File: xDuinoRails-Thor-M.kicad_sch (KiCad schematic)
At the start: 4 parts, among them J1101 Conn_01x10, J1102 Conn_01x10, J1103 Conn_01x10, U1101 MOUDLE-SEEEDUINO-XIAO

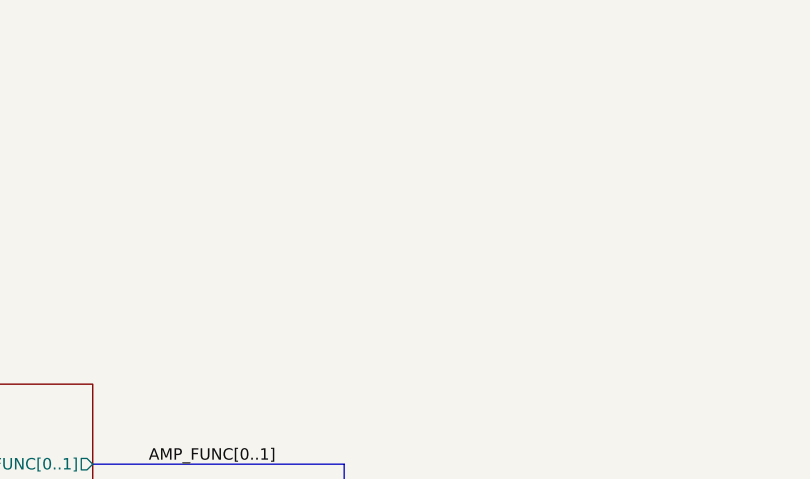
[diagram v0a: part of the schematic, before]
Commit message: Chg - Clearer PCB layout
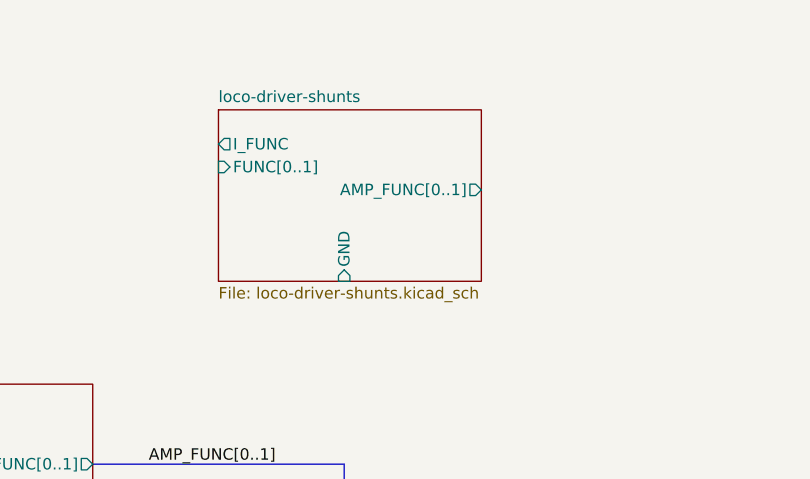
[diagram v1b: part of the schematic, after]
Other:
- added sheet loco-driver-shunts (loco-driver-shunts.kicad_sch)
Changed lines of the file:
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@@
+	)
+	(sheet
+		(at 214.63 41.91)
+		(size 29.21 19.05)
+		(fields_autoplaced yes)
+		(stroke
+			(width 0.1524)
+			(type solid)
+		)
+		(fill
+			(color 255 255 203 1.0000)
+		)
+		(property "Sheetname" "loco-driver-shunts"
+			(at 214.63 41.1984 0)
+			(effects
+				(font
+					(size 1.27 1.27)
+				)
+				(justify left bottom)
+			)
+		)
+		(property "Sheetfile" "loco-driver-shunts.kicad_sch"
+			(at 214.63 61.5446 0)
+			(effects
+				(font
+					(size 1.27 1.27)
+				)
+				(justify left top)
+			)
+		)
+		(pin "GND" input
+			(at 228.6 60.96 270)
+			(effects
+				(font
+					(size 1.27 1.27)
+				)
+				(justify left)
+			)
+		)
+		(pin "I_FUNC" output
+			(at 214.63 45.72 180)
+			(effects
+				(font
+					(size 1.27 1.27)
+				)
+				(justify left)
+			)
+		)
+		(pin "AMP_FUNC[0..1]" output
+			(at 243.84 50.8 0)
+			(effects
+				(font
+					(size 1.27 1.27)
+				)
+				(justify right)
+			)
+		)
+		(pin "FUNC[0..1]" input
+			(at 214.63 48.26 180)
+			(effects
+				(font
+					(size 1.27 1.27)
+				)
+				(justify left)
+			)
+		)
+		(instances
+			(project "xDuinoRails-Thor-M"
+				(path "/fb33ec4e-6596-45d2-a121-8d3475acd69a"
+					(page "1")
+				)
+			)
+		)
 	)
 	(sheet

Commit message: Fix - ERC updates
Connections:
- no-connect marks 6 -> 12
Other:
- sheet loco-driver-shunts ports: added +3V3, I_MOTOR, OFF_ MOTOR, OFF_FUNC; removed AMP_FUNC[0..1], FUNC[0..1]
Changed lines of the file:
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@@
 	)
 	(no_connect
+		(at 229.87 60.96)
+	)
+	(no_connect
+		(at 243.84 52.07)
+	)
+	(no_connect
 		(at 269.24 124.46)
 	)
@@
 	)
 	(no_connect
+		(at 243.84 49.53)
+	)
+	(no_connect
 		(at 269.24 129.54)
 	)
@@
 	)
 	(no_connect
+		(at 214.63 52.07)
+	)
+	(no_connect
 		(at 269.24 121.92)
 	)
 	(no_connect
+		(at 229.87 41.91)
+	)
+	(no_connect
+		(at 214.63 49.53)
+	)
+	(no_connect
 		(at 233.68 133.35)
 	)
@@
 			(project "xDuinoRails-Thor-M"
 				(path "/fb33ec4e-6596-45d2-a121-8d3475acd69a"
-					(page "11")
+					(page "2")
 				)
 			)
@@
 			(project "xDuinoRails-Thor-M"
 				(path "/fb33ec4e-6596-45d2-a121-8d3475acd69a"
-					(page "2")
+					(page "1")
 				)
 			)
@@
 			)
 		)
-		(pin "GND" input
-			(at 228.6 60.96 270)
+		(pin "I_MOTOR" input
+			(at 243.84 52.07 0)
 			(effects
 				(font
 					(size 1.27 1.27)
 				)
-				(justify left)
+				(justify right)
 			)
 		)
-		(pin "I_FUNC" output
-			(at 214.63 45.72 180)
+		(pin "+3V3" input
+			(at 229.87 41.91 90)
+			(effects
+				(font
+					(size 1.27 1.27)
+				)
+				(justify right)
+			)
+		)
+		(pin "GND" input
+			(at 229.87 60.96 270)
 			(effects
 				(font
@@
 			)
 		)
-		(pin "AMP_FUNC[0..1]" output
-			(at 243.84 50.8 0)
+		(pin "I_FUNC" input
+			(at 243.84 49.53 0)
 			(effects
 				(font
@@
 			)
 		)
-		(pin "FUNC[0..1]" input
-			(at 214.63 48.26 180)
+		(pin "OFF_ MOTOR" output
+			(at 214.63 52.07 180)
+			(effects
+				(font
+					(size 1.27 1.27)
+				)
+				(justify left)
+			)
+		)
+		(pin "OFF_FUNC" output
+			(at 214.63 49.53 180)
 			(effects
 				(font
@@
 			(project "xDuinoRails-Thor-M"
 				(path "/fb33ec4e-6596-45d2-a121-8d3475acd69a"
-					(page "1")
+					(page "11")
 				)
 			)

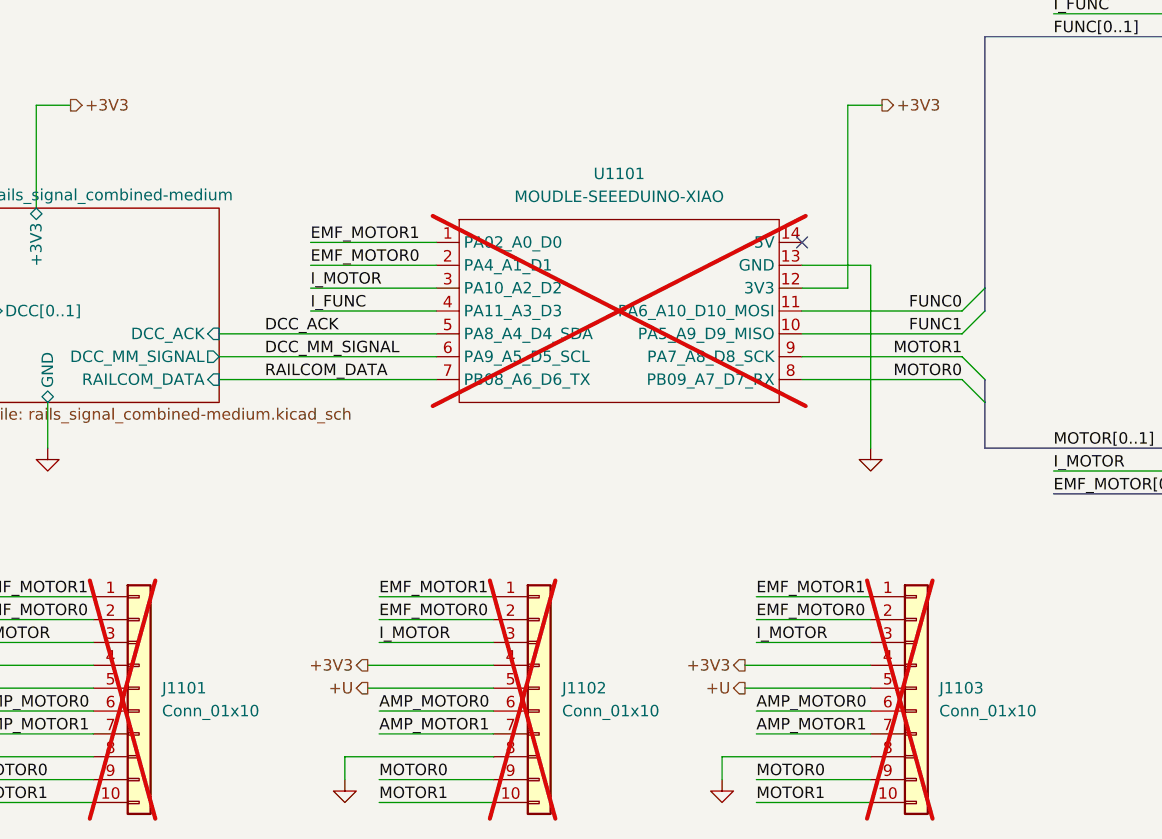
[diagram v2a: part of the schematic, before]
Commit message: Fix - Ignore double power flags
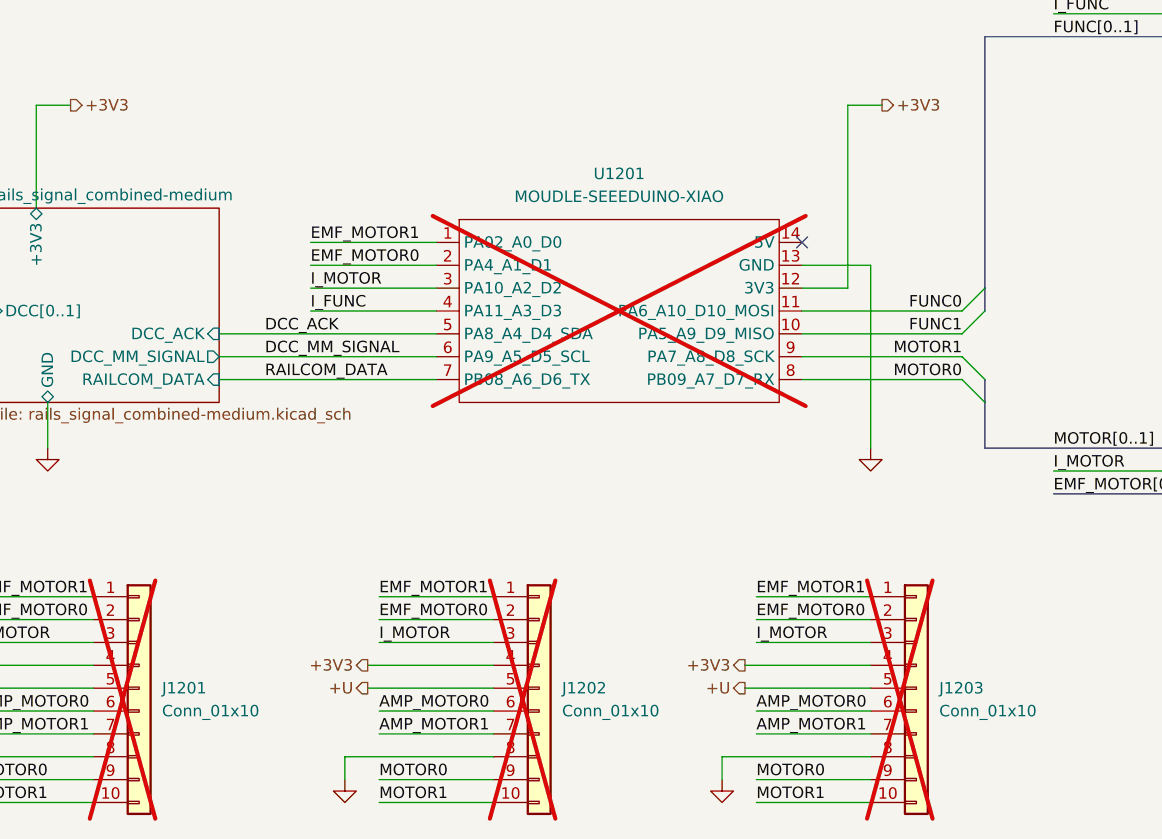
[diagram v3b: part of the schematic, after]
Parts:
- renumbered J1101 to J1201, J1102 to J1202, J1103 to J1203, U1101 to U1201
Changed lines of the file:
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@@
 		(dnp no)
 		(fields_autoplaced yes)
-		(property "Reference" "#PWR1109"
+		(property "Reference" "#PWR1209"
 			(at 27.94 167.64 0)
 			(effects
@@
 			(project "xDuinoRails-Thor-M"
 				(path "/fb33ec4e-6596-45d2-a121-8d3475acd69a"
-					(reference "#PWR1109")
+					(reference "#PWR1209")
 					(unit 1)
 				)
@@
 		(dnp no)
 		(fields_autoplaced yes)
-		(property "Reference" "#PWR1105"
+		(property "Reference" "#PWR1208"
 			(at 256.54 154.94 0)
 			(effects
@@
 			(project "xDuinoRails-Thor-M"
 				(path "/fb33ec4e-6596-45d2-a121-8d3475acd69a"
-					(reference "#PWR1105")
+					(reference "#PWR1208")
 					(unit 1)
 				)
@@
 		(dnp no)
 		(fields_autoplaced yes)
-		(property "Reference" "#PWR1108"
+		(property "Reference" "#PWR1204"
 			(at 185.42 101.6 0)
 			(effects
@@
 			(project "xDuinoRails-Thor-M"
 				(path "/fb33ec4e-6596-45d2-a121-8d3475acd69a"
-					(reference "#PWR1108")
+					(reference "#PWR1204")
 					(unit 1)
 				)
@@
 		(dnp no)
 		(fields_autoplaced yes)
-		(property "Reference" "#PWR1111"
+		(property "Reference" "#PWR1211"
 			(at 114.3 167.64 0)
 			(effects
@@
 			(project "xDuinoRails-Thor-M"
 				(path "/fb33ec4e-6596-45d2-a121-8d3475acd69a"
-					(reference "#PWR1111")
+					(reference "#PWR1211")
 					(unit 1)
 				)
@@
 		(dnp yes)
 		(fields_autoplaced yes)
-		(property "Reference" "J1101"
+		(property "Reference" "J1201"
 			(at 52.07 151.1299 0)
 			(effects
@@
 			(project ""
 				(path "/fb33ec4e-6596-45d2-a121-8d3475acd69a"
-					(reference "J1101")
+					(reference "J1201")
 					(unit 1)
 				)
@@
 		(dnp no)
 		(fields_autoplaced yes)
-		(property "Reference" "#PWR1104"
+		(property "Reference" "#PWR1207"
 			(at 179.07 146.05 0)
 			(effects
@@
 			(project "xDuinoRails-Thor-M"
 				(path "/fb33ec4e-6596-45d2-a121-8d3475acd69a"
-					(reference "#PWR1104")
+					(reference "#PWR1207")
 					(unit 1)
 				)
@@
 		(dnp yes)
 		(fields_autoplaced yes)
-		(property "Reference" "J1102"
+		(property "Reference" "J1202"
 			(at 96.52 151.1299 0)
 			(effects
@@
 			(project "xDuinoRails-Thor-M"
 				(path "/fb33ec4e-6596-45d2-a121-8d3475acd69a"
-					(reference "J1102")
+					(reference "J1202")
 					(unit 1)
 				)
@@
 		(dnp no)
 		(fields_autoplaced yes)
-		(property "Reference" "#PWR1102"
+		(property "Reference" "#PWR1202"
 			(at 44.45 72.39 0)
 			(effects
@@
 			(project "xDuinoRails-Hermes-M"
 				(path "/fb33ec4e-6596-45d2-a121-8d3475acd69a"
-					(reference "#PWR1102")
+					(reference "#PWR1202")
 					(unit 1)
 				)
@@
 		(dnp no)
 		(fields_autoplaced yes)
-		(property "Reference" "#PWR1103"
+		(property "Reference" "#PWR1203"
 			(at 144.78 72.39 0)
 			(effects
@@
 			(project "xDuinoRails-Hermes-M"
 				(path "/fb33ec4e-6596-45d2-a121-8d3475acd69a"
-					(reference "#PWR1103")
+					(reference "#PWR1203")
 					(unit 1)
 				)
@@
 		(dnp no)
 		(fields_autoplaced yes)
-		(property "Reference" "#PWR1106"
+		(property "Reference" "#PWR1205"
 			(at 39.37 130.81 0)
 			(effects
@@
 			(project "xDuinoRails-Hermes-M"
 				(path "/fb33ec4e-6596-45d2-a121-8d3475acd69a"
-					(reference "#PWR1106")
+					(reference "#PWR1205")
 					(unit 1)
 				)
@@
 		(dnp no)
 		(fields_autoplaced yes)
-		(property "Reference" "#PWR1101"
+		(property "Reference" "#PWR1201"
 			(at 100.33 71.12 0)
 			(effects
@@
 			(project "xDuinoRails-Thor-M"
 				(path "/fb33ec4e-6596-45d2-a121-8d3475acd69a"
-					(reference "#PWR1101")
+					(reference "#PWR1201")
 					(unit 1)
 				)
@@
 		(dnp no)
 		(fields_autoplaced yes)
-		(property "Reference" "#PWR1110"
+		(property "Reference" "#PWR1210"
 			(at 72.39 167.64 0)
 			(effects
@@
 			(project "xDuinoRails-Thor-M"
 				(path "/fb33ec4e-6596-45d2-a121-8d3475acd69a"
-					(reference "#PWR1110")
+					(reference "#PWR1210")
 					(unit 1)
 				)
@@
 		(dnp yes)
 		(fields_autoplaced yes)
-		(property "Reference" "U1101"
+		(property "Reference" "U1201"
 			(at 102.87 93.98 0)
 			(effects
@@
 			(project ""
 				(path "/fb33ec4e-6596-45d2-a121-8d3475acd69a"
-					(reference "U1101")
+					(reference "U1201")
 					(unit 1)
 				)
@@
 		(dnp yes)
 		(fields_autoplaced yes)
-		(property "Reference" "J1103"
+		(property "Reference" "J1203"
 			(at 138.43 151.1299 0)
 			(effects
@@
 			(project "xDuinoRails-Thor-M"
 				(path "/fb33ec4e-6596-45d2-a121-8d3475acd69a"
-					(reference "J1103")
+					(reference "J1203")
 					(unit 1)
 				)
@@
 		(dnp no)
 		(fields_autoplaced yes)
-		(property "Reference" "#PWR1107"
+		(property "Reference" "#PWR1206"
 			(at 130.81 130.81 0)
 			(effects
@@
 			(project "xDuinoRails-Hermes-S"
 				(path "/fb33ec4e-6596-45d2-a121-8d3475acd69a"
-					(reference "#PWR1107")
-					(unit 1)
-				)
+					(reference "#PWR1206")
+					(unit 1)
+				)
